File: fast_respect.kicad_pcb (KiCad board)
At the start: 2 copper layers, 70 x 110 mm, 97 parts, among them J1_1 Conn_02x04_Odd_Even, J5_1 Conn_02x03_Odd_Even, J5_2 Conn_02x03_Odd_Even, J7_1 Conn_01x02, Q2_1 IRLML6402, Q3_1 IRLML6344T, Q4_1 IRLML6344T, Q4_2 IRLML6344T, Q4_3 IRLML6344T, Q4_4 IRLML6344T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

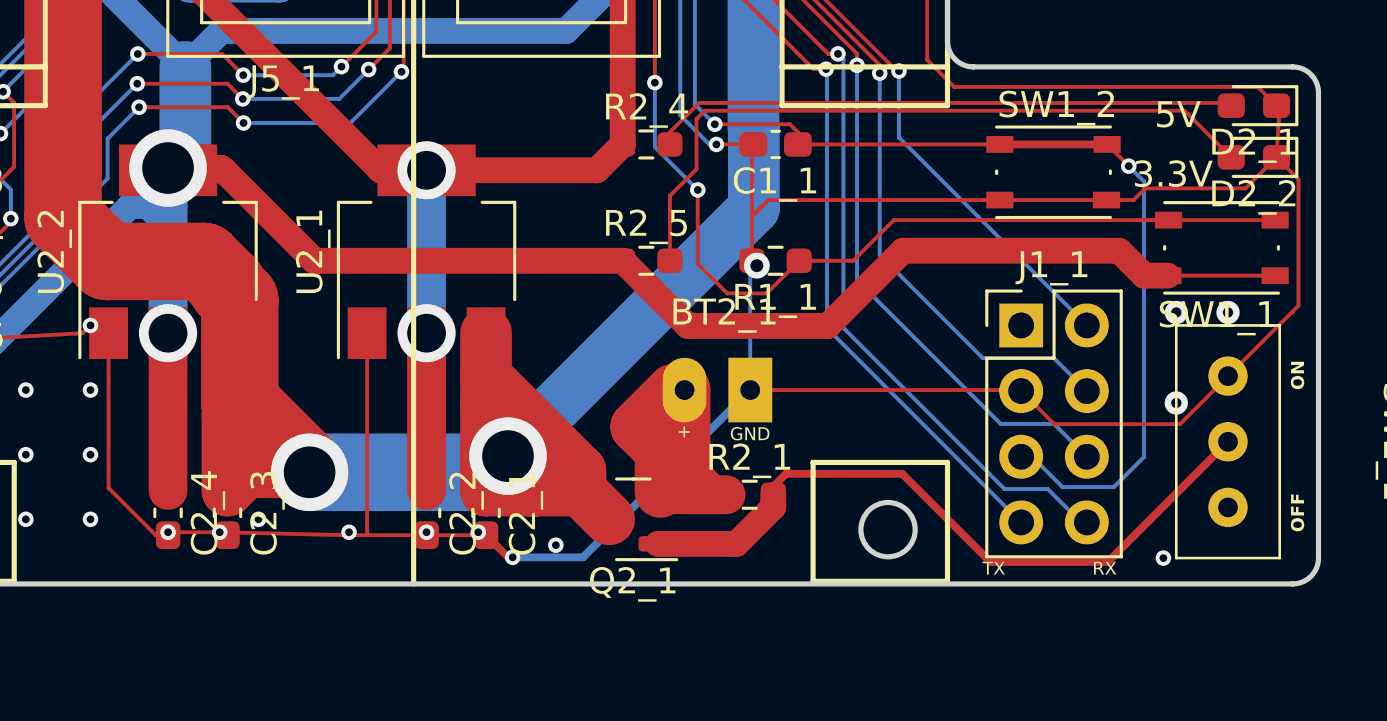
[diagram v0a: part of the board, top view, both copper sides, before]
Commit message: ベタグランドのために電源周り位置変えた
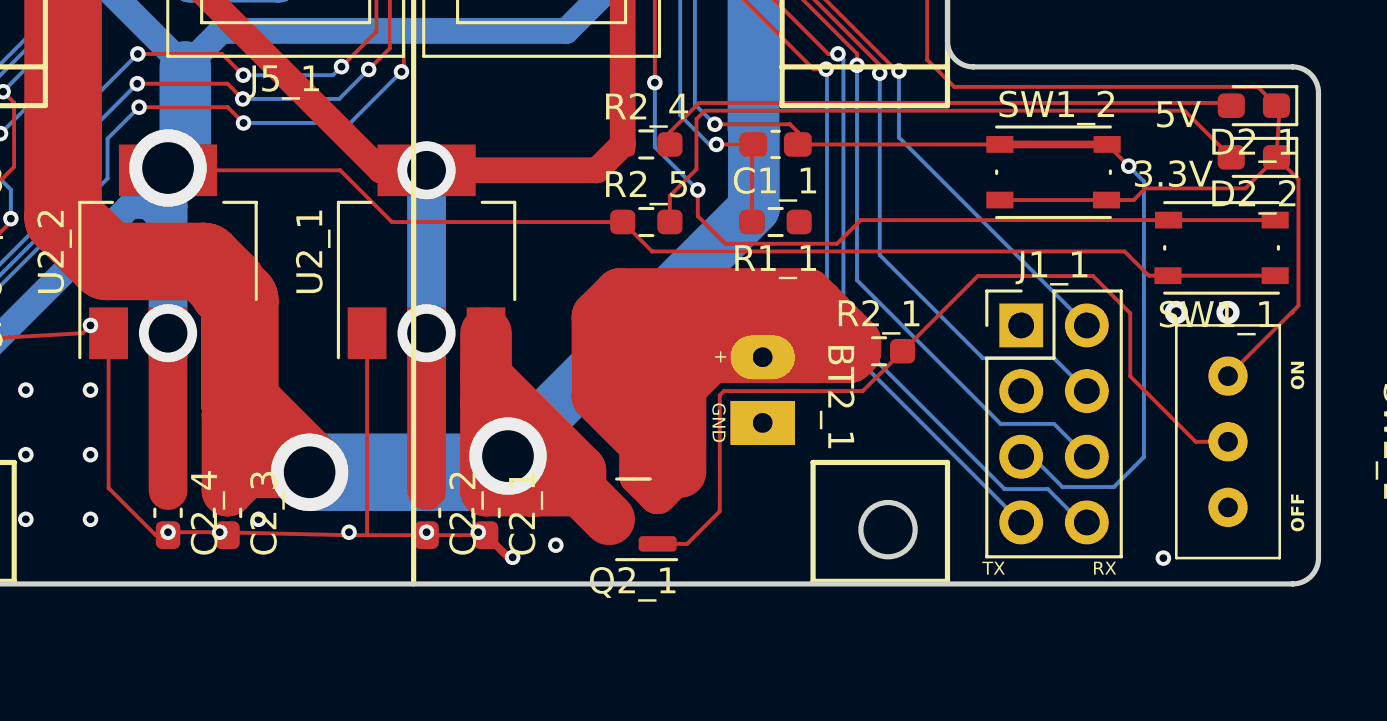
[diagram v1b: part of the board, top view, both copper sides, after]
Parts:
- moved R2_1 7.47 mm to (-17.0, 101.0)
- moved BT2_1 1.75 mm to (-21.5, 102.5), turned to -90 degrees
- moved R1_1 1.50 mm to (-21.0, 96.0)
- moved R2_5 1.50 mm to (-26.0, 96.0)
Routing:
- net Net-(BT2_1-+): track 14.0 -> 70.3 mm
- net GND: track 571.7 -> 523.4 mm, vias 96 -> 94
- net +3.3V: track 412.0 -> 402.4 mm
- net Net-(Q2_1-G): track 27.0 -> 33.1 mm
- net BOOT0: track 71.2 -> 68.5 mm
- net Net-(D2_2-A): track 27.5 -> 26.0 mm

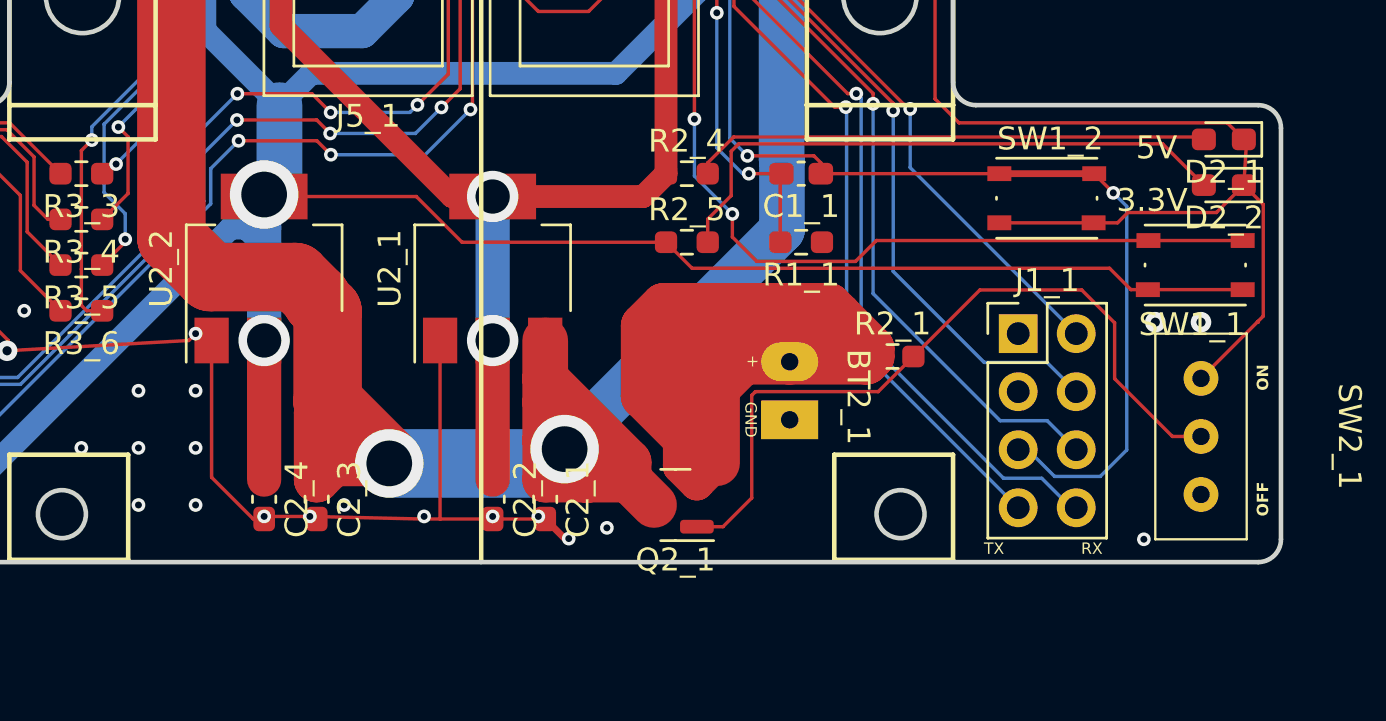
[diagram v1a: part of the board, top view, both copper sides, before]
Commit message: 電源周りを変えて更にベタに強くした
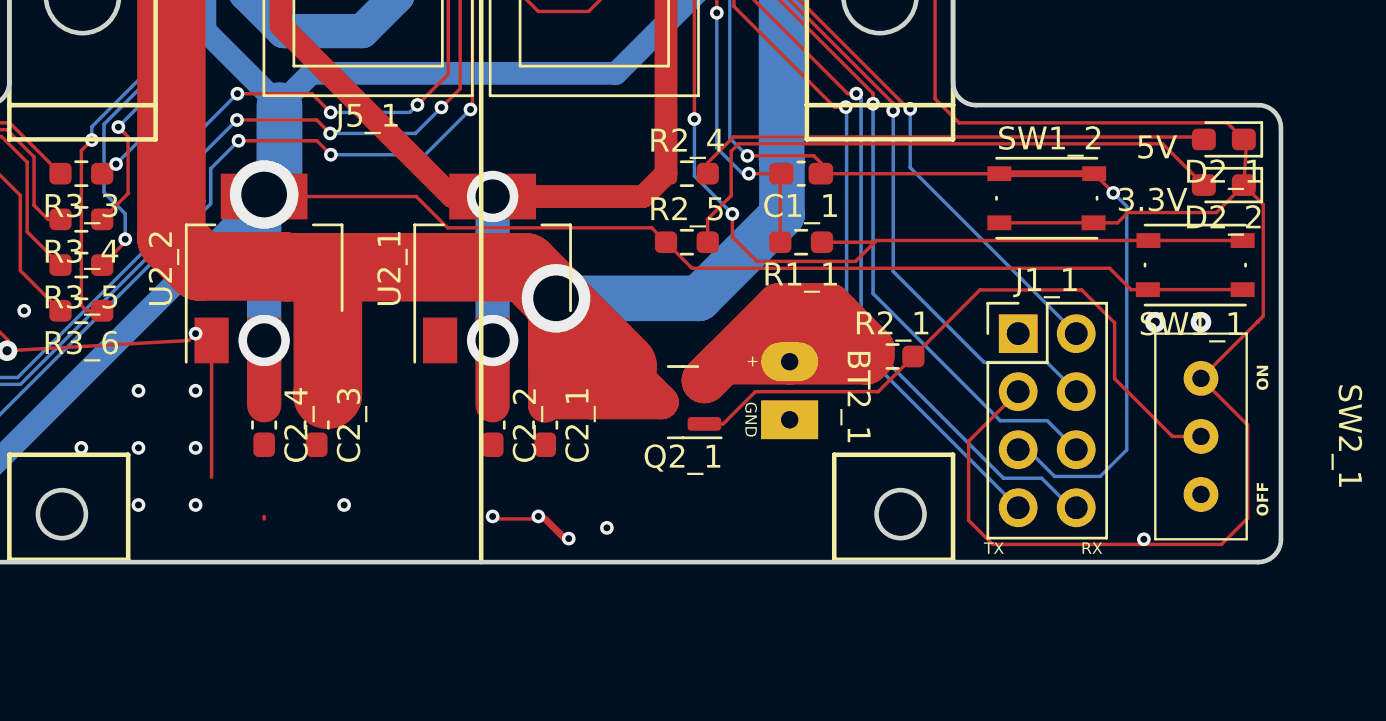
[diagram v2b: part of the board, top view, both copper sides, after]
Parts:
- moved Q2_1 4.51 mm to (-26.2, 103.0)
- moved C2_1 3.25 mm to (-32.2, 104.0)
- moved C2_2 3.25 mm to (-34.5, 104.0)
- moved C2_3 3.25 mm to (-42.2, 104.0)
- moved C2_4 3.25 mm to (-44.5, 104.0)
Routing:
- net Net-(BT2_1-+): track 70.3 -> 21.4 mm
- net +8V: track 178.9 -> 168.9 mm, vias 3 -> 2
- net GND: track 523.4 -> 529.1 mm, vias 94 -> 91
- net Net-(Q2_1-G): track 33.1 -> 28.2 mm
- net +5V: track 51.2 -> 48.0 mm
- net +3.3V: track 402.4 -> 399.2 mm
- net BOOT0: track 68.5 -> 70.9 mm

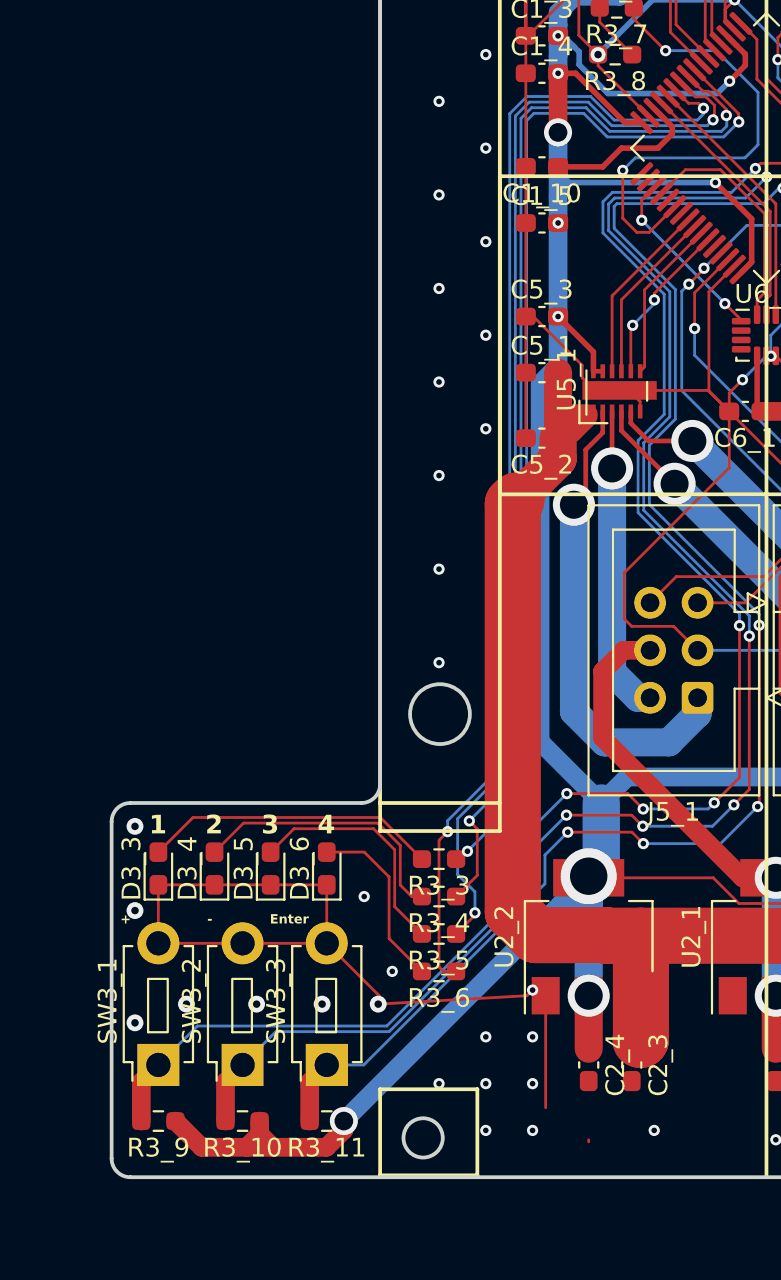
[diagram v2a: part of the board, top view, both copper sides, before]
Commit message: UIスイッチ周りを整えてベタ強化
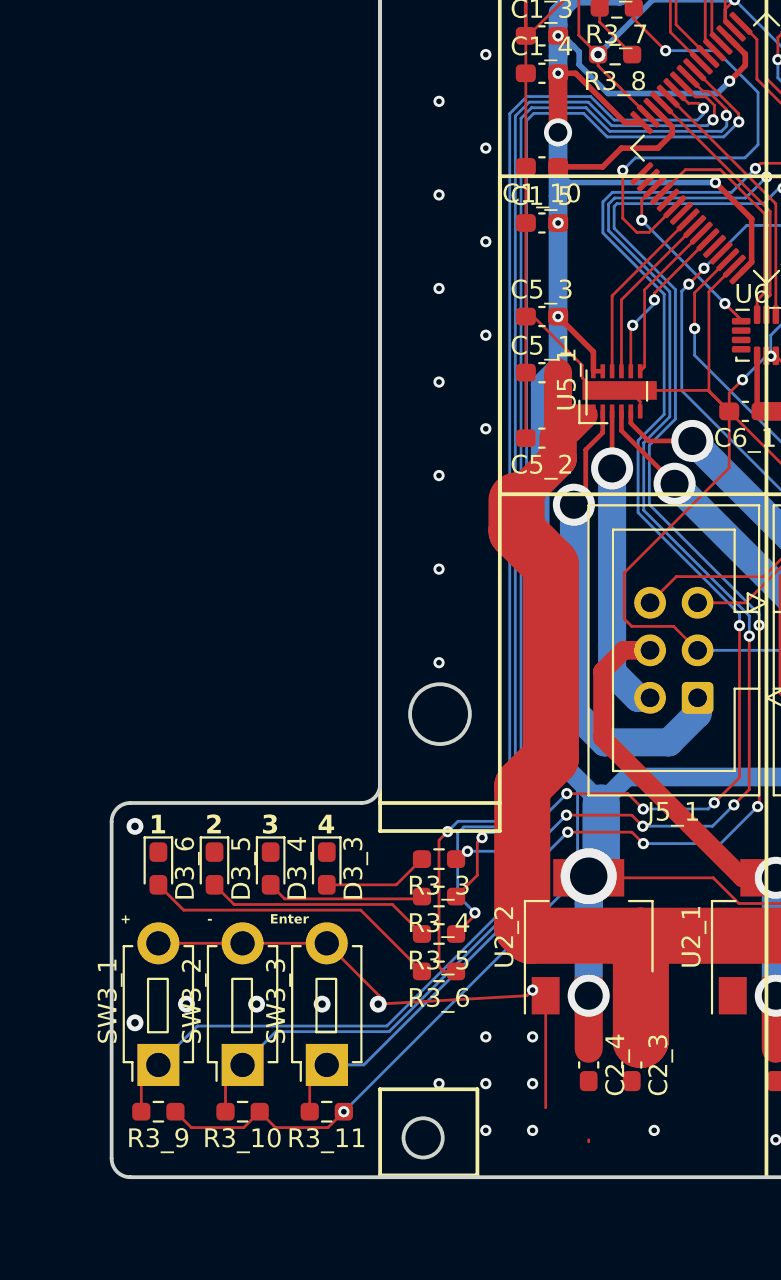
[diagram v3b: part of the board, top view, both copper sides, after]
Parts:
- moved D3_3 9.00 mm to (-58.5, 93.5), turned to -90 degrees
- moved D3_6 9.00 mm to (-67.5, 93.5), turned to -90 degrees
- moved D3_4 3.00 mm to (-61.5, 93.5), turned to -90 degrees
- moved D3_5 3.00 mm to (-64.5, 93.5), turned to -90 degrees
- moved R3_10 0.50 mm to (-63.0, 106.5)
- moved R3_11 0.50 mm to (-58.5, 106.5)
- moved R3_9 0.50 mm to (-67.5, 106.5)
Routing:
- net GND: track 529.1 -> 513.9 mm, vias 91 -> 88
- net Net-(D3_3-A): track 15.8 -> 5.66 mm
- net Net-(D3_6-A): track 9.66 -> 16.0 mm
- net Net-(D3_4-A): track 14.6 -> 8.45 mm
- net +3.3V: track 399.2 -> 402.5 mm
- net UI_LED_4: track 61.8 -> 63.2 mm
- net +8V: track 168.9 -> 170.2 mm
- net UI_LED_3: track 60.4 -> 61.6 mm
- net UI_LED_1: track 57.3 -> 58.1 mm
- net Net-(D3_5-A): track 12.7 -> 12.2 mm
- net UI_SW_3: track 83.8 -> 83.3 mm
- net UI_SW_2: track 88.7 -> 88.2 mm

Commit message: 配線を完全に完了した。ベタグランドのビアはこれから打つ
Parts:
- moved SW1_2 1.42 mm to (-10.2, 95.5), turned to 180 degrees
- moved D2_1 1.35 mm to (-3.75, 92.0)
- moved D2_2 1.35 mm to (-3.75, 94.0)
- moved C1_1 1.00 mm to (-21.0, 94.0)
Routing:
- net SWCLK: track 48.9 -> 53.5 mm
- net Net-(D2_2-A): track 26.0 -> 23.5 mm
- net SWDIO: track 57.1 -> 58.9 mm
- net BOOT0: track 70.9 -> 69.9 mm
- net Net-(D2_1-A): track 22.7 -> 21.7 mm
- net GND: track 513.9 -> 513.0 mm
- net NRST: track 78.5 -> 77.8 mm
- net SWO: track 57.9 -> 58.4 mm

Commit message: ビア打つところまで完全に完了したと思う
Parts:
- moved SW1_1 0.50 mm to (-4.25, 97.0)
- moved SW2_1 0.25 mm to (-3.75, 104.5)
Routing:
- net GND: track 513.0 -> 533.5 mm, vias 88 -> 194
- net Net-(Q2_1-G): track 28.2 -> 27.4 mm
- net NRST: track 77.8 -> 77.1 mm
- net +3.3V: track 402.5 -> 402.0 mm

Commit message: ビア打ち直した。これから浮島とかノイズ原因に鳴る半島を削除したい。
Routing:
- net (no net): track 2.90 -> 0.00 mm
- net GND: track 533.5 -> 533.8 mm, vias 194 -> 241

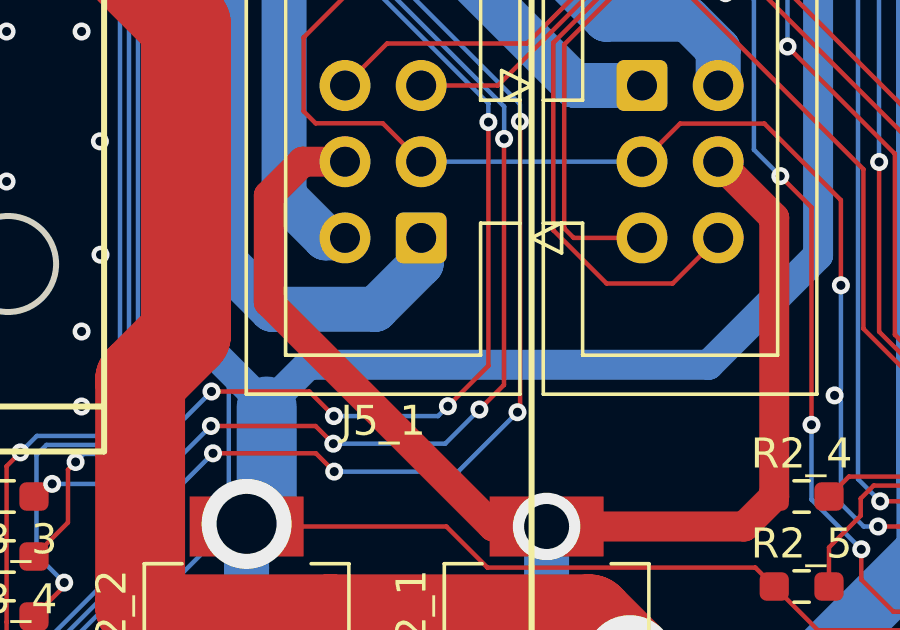
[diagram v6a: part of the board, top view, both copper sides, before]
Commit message: ビアを１つ新たに打った。とりあえずシルクとかのエラーを消したい。
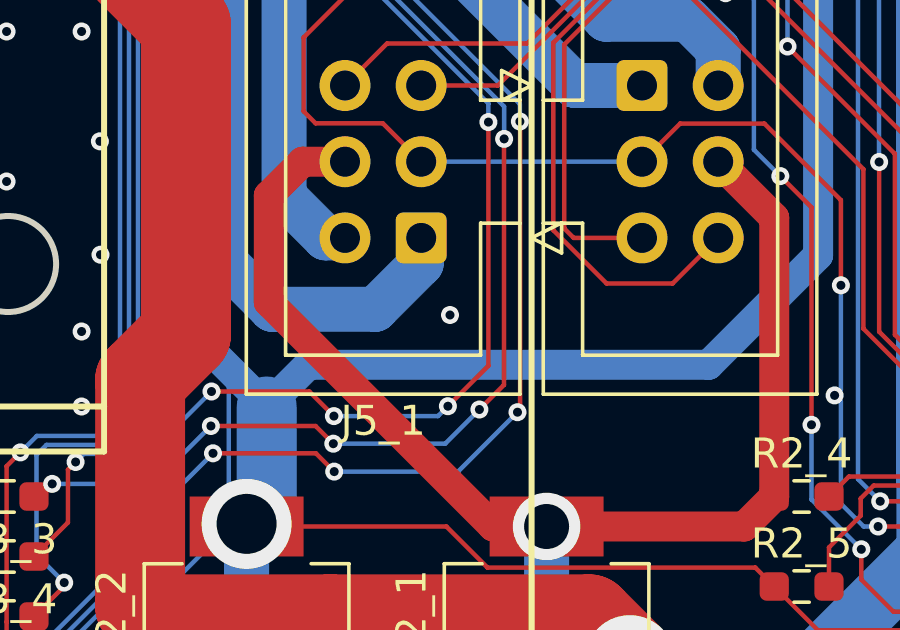
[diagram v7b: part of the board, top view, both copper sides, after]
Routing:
- net GND: vias 241 -> 242
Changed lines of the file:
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@@
   (via (at -44.69 18) (size 0.6) (drill 0.3) (layers "F.Cu" "B.Cu") (net 6))
   (via (at -37.67 64.52) (size 0.6) (drill 0.3) (layers "F.Cu" "B.Cu") (free) (net 6))
+  (via (at -37.72 86.95) (size 0.6) (drill 0.3) (layers "F.Cu" "B.Cu") (free) (net 6))
   (via (at -48 49) (size 0.6) (drill 0.3) (layers "F.Cu" "B.Cu") (net 6))
   (via (at -43.5 36) (size 0.6) (drill 0.3) (layers "F.Cu" "B.Cu") (free) (net 6))

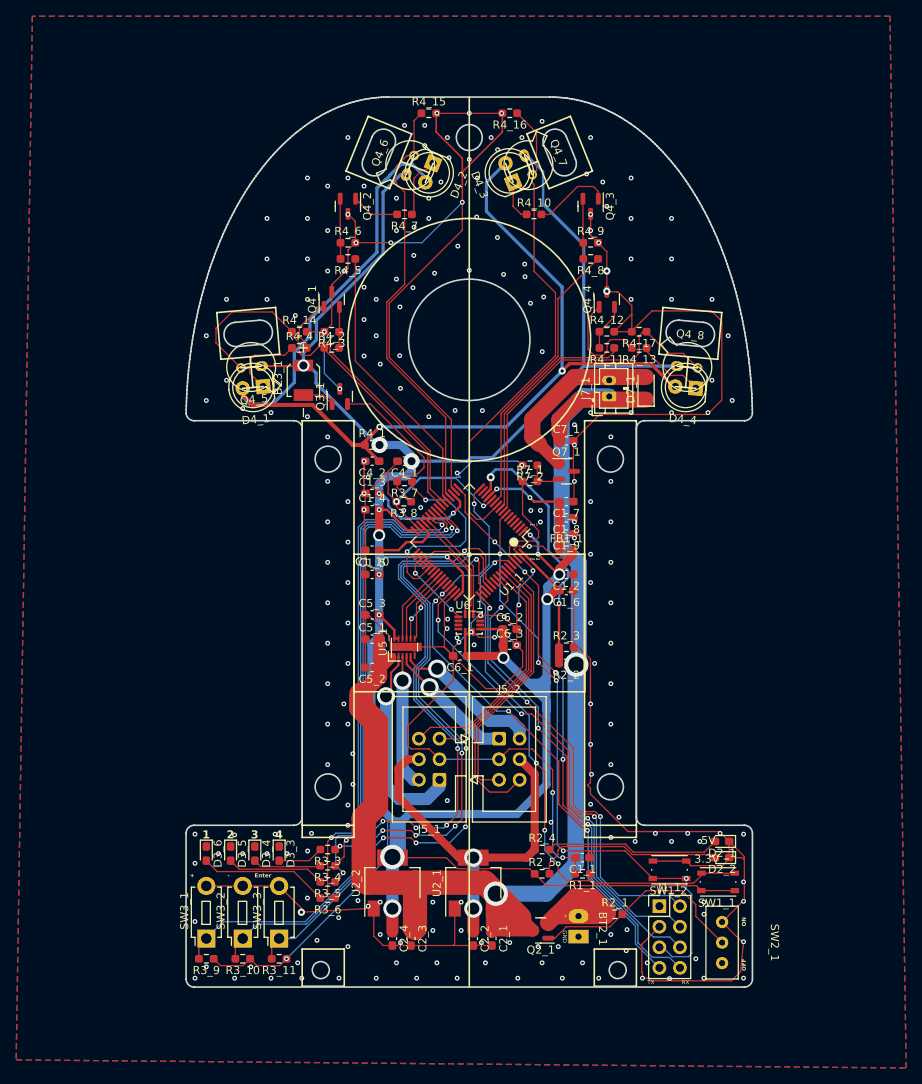
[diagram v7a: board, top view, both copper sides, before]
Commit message: 色々と文字とかのプリント関係を直したが、これ以上は無視設定が必要そう（Fabの値とシルクがかぶる）
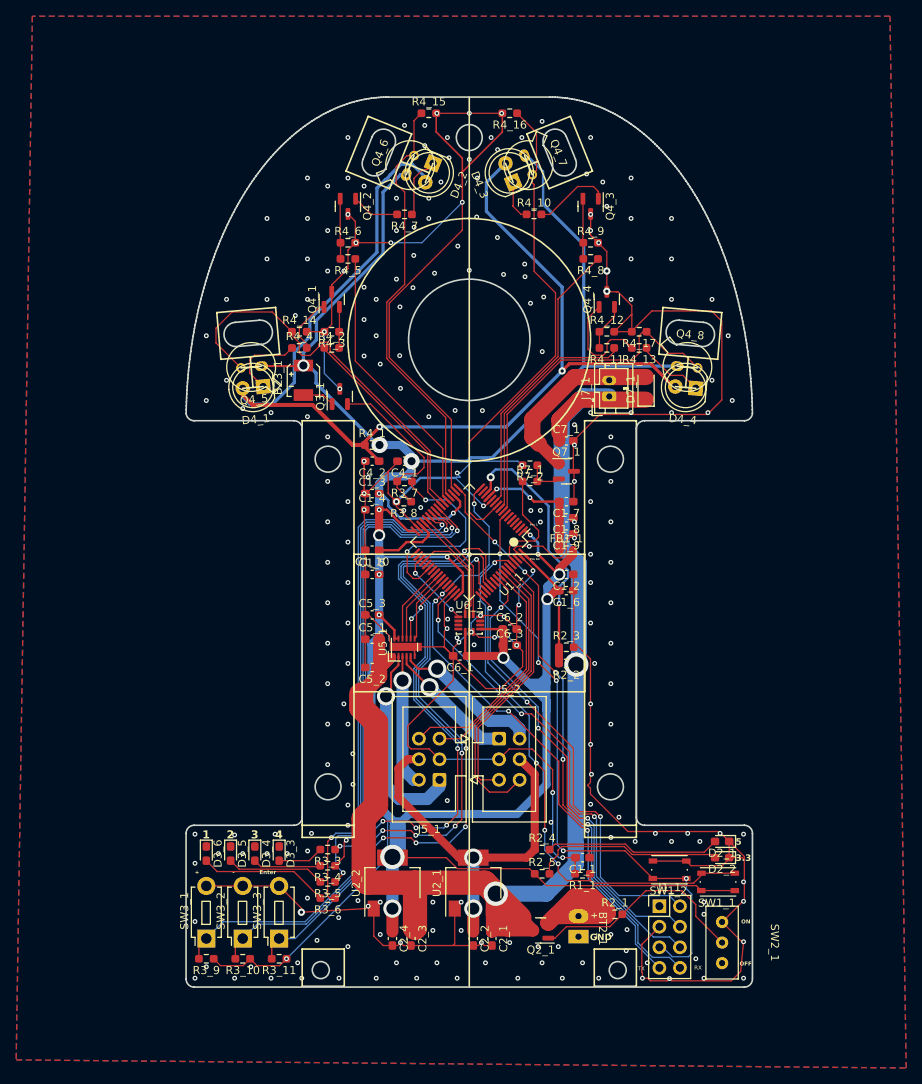
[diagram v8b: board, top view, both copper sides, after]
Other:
- board text added: "3.3"
- board text added: "5"
- board text removed: "3.3V"
- board text removed: "5V"
